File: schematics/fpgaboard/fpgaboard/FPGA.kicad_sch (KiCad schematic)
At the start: 15 parts, among them J1 SODIMM-200, U1 LFE5UM-85F-8BG381I, U13 W25Q32JVSS

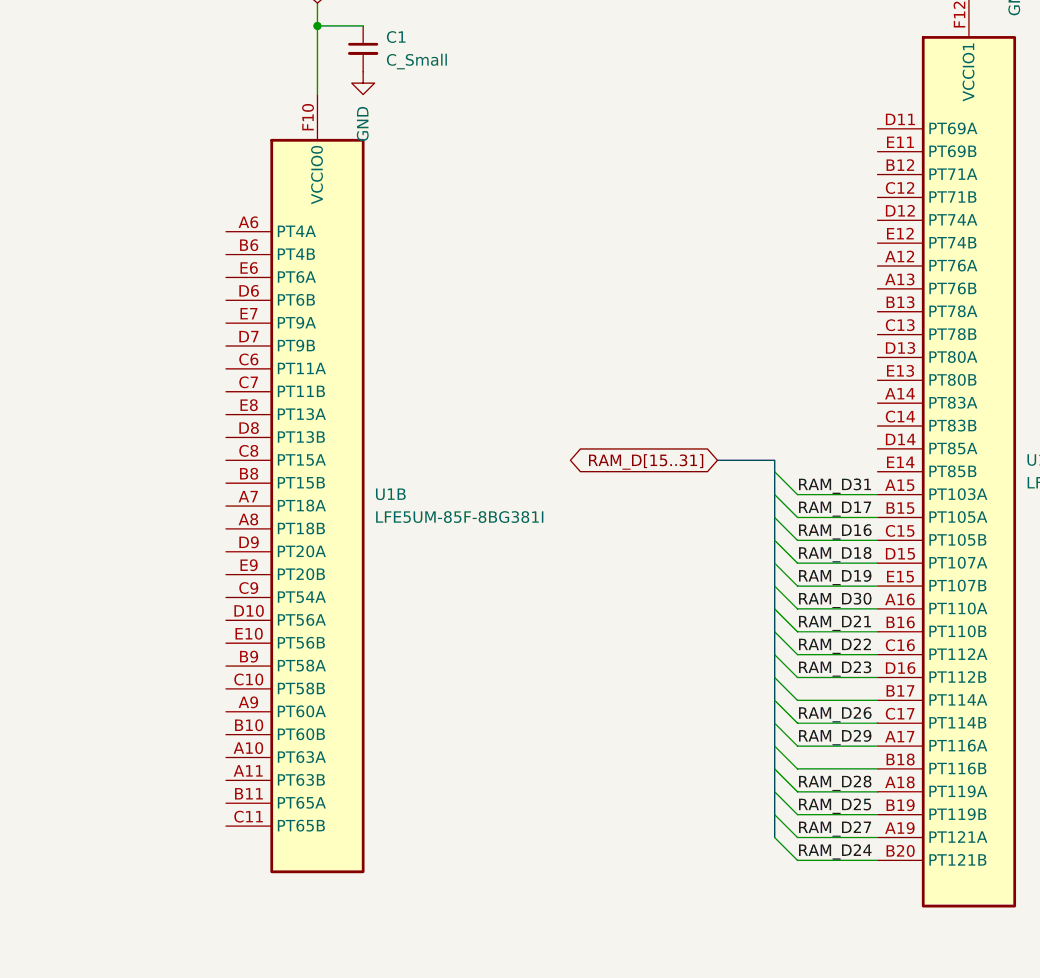
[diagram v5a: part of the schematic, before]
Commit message: Begun working on FPGA board SODIMM bottom routing.
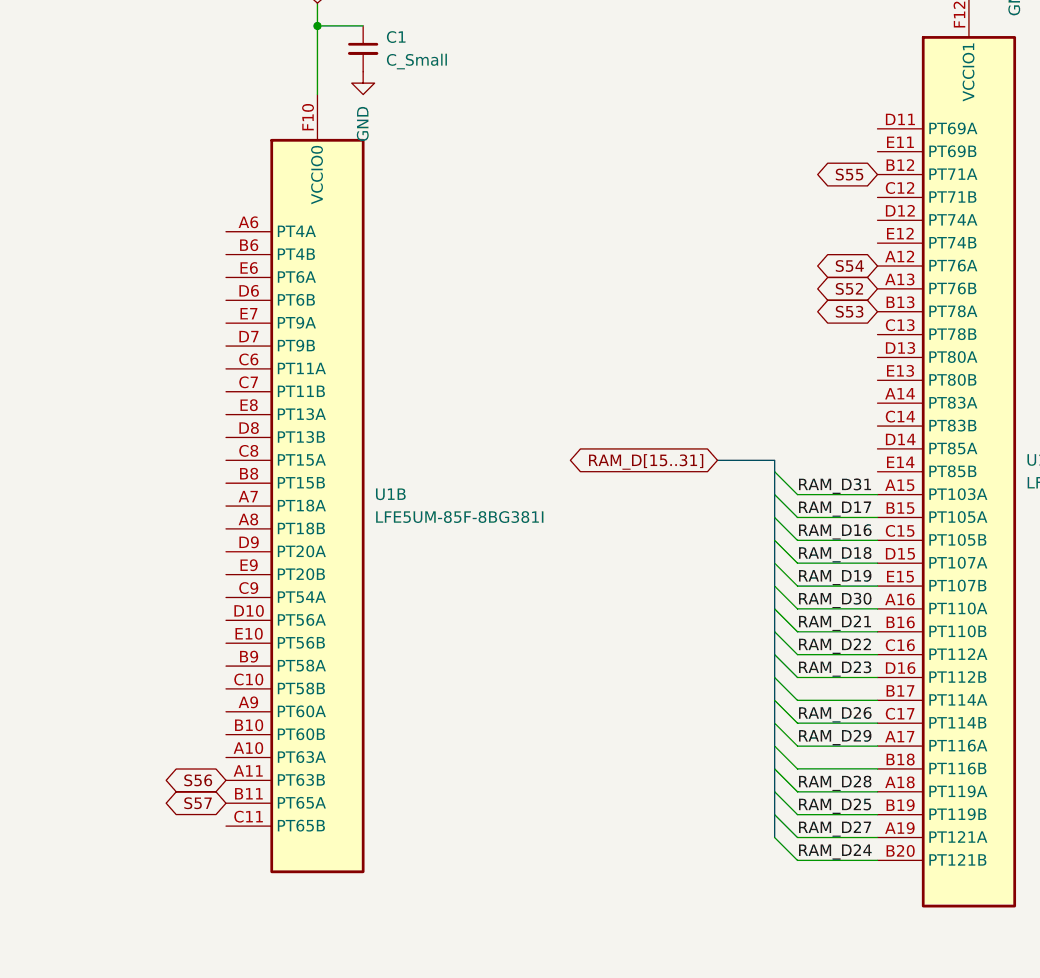
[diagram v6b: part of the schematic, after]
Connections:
- net S52: now also U1.A13 (PT76B)
- net S53: now also U1.B13 (PT78A)
- net S54: now also U1.A12 (PT76A)
- net S55: now also U1.B12 (PT71A)
- net S56: now also U1.A11 (PT63B)
- net S57: now also U1.B11 (PT65A)
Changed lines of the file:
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@@
 		)
 	)
+	(global_label "S54"
+		(shape bidirectional)
+		(at 120.65 77.47 180)
+		(fields_autoplaced yes)
+		(effects
+			(font
+				(size 1.27 1.27)
+			)
+			(justify right)
+		)
+		(property "Intersheetrefs" "${INTERSHEET_REFS}"
+			(at 112.925 77.47 0)
+			(effects
+				(font
+					(size 1.27 1.27)
+				)
+				(justify right)
+				(hide yes)
+			)
+		)
+	)
 	(global_label "FLASH_IO3"
 		(shape bidirectional)
@@
 		)
 	)
+	(global_label "S57"
+		(shape bidirectional)
+		(at 48.26 137.16 180)
+		(fields_autoplaced yes)
+		(effects
+			(font
+				(size 1.27 1.27)
+			)
+			(justify right)
+		)
+		(property "Intersheetrefs" "${INTERSHEET_REFS}"
+			(at 40.535 137.16 0)
+			(effects
+				(font
+					(size 1.27 1.27)
+				)
+				(justify right)
+				(hide yes)
+			)
+		)
+	)
 	(global_label "JTAG_TDI"
 		(shape input)
@@
 		)
 	)
+	(global_label "S53"
+		(shape bidirectional)
+		(at 120.65 82.55 180)
+		(fields_autoplaced yes)
+		(effects
+			(font
+				(size 1.27 1.27)
+			)
+			(justify right)
+		)
+		(property "Intersheetrefs" "${INTERSHEET_REFS}"
+			(at 112.925 82.55 0)
+			(effects
+				(font
+					(size 1.27 1.27)
+				)
+				(justify right)
+				(hide yes)
+			)
+		)
+	)
 	(global_label "S38"
 		(shape bidirectional)
@@
 		)
 	)
+	(global_label "S55"
+		(shape bidirectional)
+		(at 120.65 67.31 180)
+		(fields_autoplaced yes)
+		(effects
+			(font
+				(size 1.27 1.27)
+			)
+			(justify right)
+		)
+		(property "Intersheetrefs" "${INTERSHEET_REFS}"
+			(at 112.925 67.31 0)
+			(effects
+				(font
+					(size 1.27 1.27)
+				)
+				(justify right)
+				(hide yes)
+			)
+		)
+	)
 	(global_label "S99"
 		(shape bidirectional)
@@
 		)
 	)
+	(global_label "S52"
+		(shape bidirectional)
+		(at 120.65 80.01 180)
+		(fields_autoplaced yes)
+		(effects
+			(font
+				(size 1.27 1.27)
+			)
+			(justify right)
+		)
+		(property "Intersheetrefs" "${INTERSHEET_REFS}"
+			(at 112.925 80.01 0)
+			(effects
+				(font
+					(size 1.27 1.27)
+				)
+				(justify right)
+				(hide yes)
+			)
+		)
+	)
 	(global_label "~{RAM_RAS}"
 		(shape output)
@@
 			(effects
 				(font
+					(size 1.27 1.27)
+				)
+				(justify right)
+				(hide yes)
+			)
+		)
+	)
+	(global_label "S56"
+		(shape bidirectional)
+		(at 48.26 134.62 180)
+		(fields_autoplaced yes)
+		(effects
+			(font
+				(size 1.27 1.27)
+			)
+			(justify right)
+		)
+		(property "Intersheetrefs" "${INTERSHEET_REFS}"
+			(at 40.535 134.62 0)
+			(effects
+				(font

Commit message: More work on FPGA board.
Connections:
- net S58: now also U1.A10 (PT63A)
- net S59: now also U1.B10 (PT60B)
- net S60: now also U1.A9 (PT60A)
- net S61: now also U1.B9 (PT58A)
- net S62: now also U1.A8 (PT18B)
- net S63: now also U1.B8 (PT15B)
- net S64: now also U1.A7 (PT18A)
- net S65: now also U1.C7 (PT11B)
- net S66: now also U1.A6 (PT4A)
- net S67: now also U1.B6 (PT4B)
- net S68: now also U1.B5 (PL11C)
- net S69: now also U1.C5 (PL11D)
- net S70: now also U1.C6 (PT11A)
- net S71: now also U1.D6 (PT6B)
- net S72: now also U1.E5 (PL20C)
- net S73: now also U1.F5 (PL20D)
- net S74: now also U1.H5 (PL41C), U1.J4 (PL50A)
- net S75: now also U1.K3 (PL50D)
- net S76: now also U1.L3 (PL86C)
- net S77: now also U1.M4 (PL83A)
- net S78: now also U1.N3 (PL86A)

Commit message: Some work on FPGA board.
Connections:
- net S74: no longer U1.J4 (PL50A)
- net S75: now also U1.J4 (PL50A); no longer U1.K3 (PL50D)
- net S76: now also U1.K3 (PL50D); no longer U1.L3 (PL86C)
- net S77: now also U1.K4 (PL56A); no longer U1.M4 (PL83A)
- net S78: now also U1.L3 (PL86C); no longer U1.N3 (PL86A)
- net S79: now also U1.L4 (PL56C)
- net S80: now also U1.M4 (PL83A)
- net S81: now also U1.N3 (PL86A)
- net S82: now also U1.N4 (PL83C)
- net S83: now also U1.N5 (PL83B)
- net S84: now also U1.P5 (PL83D)
- net S85: now also U1.E6 (PT6A)
- net S86: now also U1.D7 (PT9B)
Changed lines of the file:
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@@
 		)
 	)
+	(global_label "S80"
+		(shape bidirectional)
+		(at 341.63 107.95 180)
+		(fields_autoplaced yes)
+		(effects
+			(font
+				(size 1.27 1.27)
+			)
+			(justify right)
+		)
+		(property "Intersheetrefs" "${INTERSHEET_REFS}"
+			(at 333.905 107.95 0)
+			(effects
+				(font
+					(size 1.27 1.27)
+				)
+				(justify right)
+				(hide yes)
+			)
+		)
+	)
 	(global_label "S29"
 		(shape bidirectional)
@@
 		)
 	)
-	(global_label "S74"
+	(global_label "S75"
 		(shape bidirectional)
 		(at 341.63 74.93 180)
@@
 		)
 	)
+	(global_label "S86"
+		(shape bidirectional)
+		(at 48.26 86.36 180)
+		(fields_autoplaced yes)
+		(effects
+			(font
+				(size 1.27 1.27)
+			)
+			(justify right)
+		)
+		(property "Intersheetrefs" "${INTERSHEET_REFS}"
+			(at 40.535 86.36 0)
+			(effects
+				(font
+					(size 1.27 1.27)
+				)
+				(justify right)
+				(hide yes)
+			)
+		)
+	)
 	(global_label "S63"
 		(shape bidirectional)
@@
 		)
 	)
+	(global_label "S81"
+		(shape bidirectional)
+		(at 341.63 118.11 180)
+		(fields_autoplaced yes)
+		(effects
+			(font
+				(size 1.27 1.27)
+			)
+			(justify right)
+		)
+		(property "Intersheetrefs" "${INTERSHEET_REFS}"
+			(at 333.905 118.11 0)
+			(effects
+				(font
+					(size 1.27 1.27)
+				)
+				(justify right)
+				(hide yes)
+			)
+		)
+	)
 	(global_label "S17"
 		(shape bidirectional)
@@
 		)
 	)
+	(global_label "S84"
+		(shape bidirectional)
+		(at 341.63 115.57 180)
+		(fields_autoplaced yes)
+		(effects
+			(font
+				(size 1.27 1.27)
+			)
+			(justify right)
+		)
+		(property "Intersheetrefs" "${INTERSHEET_REFS}"
+			(at 333.905 115.57 0)
+			(effects
+				(font
+					(size 1.27 1.27)
+				)
+				(justify right)
+				(hide yes)
+			)
+		)
+	)
 	(global_label "S26"
 		(shape bidirectional)
@@
 		)
 	)
+	(global_label "S85"
+		(shape bidirectional)
+		(at 48.26 78.74 180)
+		(fields_autoplaced yes)
+		(effects
+			(font
+				(size 1.27 1.27)
+			)
+			(justify right)
+		)
+		(property "Intersheetrefs" "${INTERSHEET_REFS}"
+			(at 40.535 78.74 0)
+			(effects
+				(font
+					(size 1.27 1.27)
+				)
+				(justify right)
+				(hide yes)
+			)
+		)
+	)
 	(global_label "S36"
 		(shape bidirectional)
@@
 		)
 	)
+	(global_label "S83"
+		(shape bidirectional)
+		(at 341.63 110.49 180)
+		(fields_autoplaced yes)
+		(effects
+			(font
+				(size 1.27 1.27)
+			)
+			(justify right)
+		)
+		(property "Intersheetrefs" "${INTERSHEET_REFS}"
+			(at 333.905 110.49 0)
+			(effects
+				(font
+					(size 1.27 1.27)
+				)
+				(justify right)
+				(hide yes)
+			)
+		)
+	)
 	(global_label "1v1"
 		(shape input)
@@
 		)
 	)
-	(global_label "S76"
+	(global_label "S77"
 		(shape bidirectional)
-		(at 341.63 123.19 180)
+		(at 341.63 95.25 180)
 		(fields_autoplaced yes)
 		(effects
@@
 		)
 		(property "Intersheetrefs" "${INTERSHEET_REFS}"
-			(at 333.905 123.19 0)
+			(at 333.905 95.25 0)
 			(effects
 				(font
@@
 		)
 	)
+	(global_label "S82"
+		(shape bidirectional)
+		(at 341.63 113.03 180)
+		(fields_autoplaced yes)
+		(effects
+			(font
+				(size 1.27 1.27)
+			)
+			(justify right)
+		)
+		(property "Intersheetrefs" "${INTERSHEET_REFS}"
+			(at 333.905 113.03 0)
+			(effects
+				(font
+					(size 1.27 1.27)
+				)
+				(justify right)
+				(hide yes)
+			)
+		)
+	)
 	(global_label "S83"
 		(shape bidirectional)
@@
 		)
 	)
-	(global_label "S78"
+	(global_label "S79"
 		(shape bidirectional)
-		(at 341.63 118.11 180)
+		(at 341.63 100.33 180)
 		(fields_autoplaced yes)
 		(effects
@@
 		)
 		(property "Intersheetrefs" "${INTERSHEET_REFS}"
-			(at 333.905 118.11 0)
+			(at 333.905 100.33 0)
 			(effects
 				(font
@@
 		)
 	)
-	(global_label "S75"
+	(global_label "S76"
 		(shape bidirectional)
 		(at 341.63 82.55 180)
@@
 		)
 	)
-	(global_label "S77"
+	(global_label "S78"
 		(shape bidirectional)
-		(at 341.63 107.95 180)
+		(at 341.63 123.19 180)
 		(fields_autoplaced yes)
 		(effects
@@
 		)
 		(property "Intersheetrefs" "${INTERSHEET_REFS}"
-			(at 333.905 107.95 0)
+			(at 333.905 123.19 0)
 			(effects
 				(font
